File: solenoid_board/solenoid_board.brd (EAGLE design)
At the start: 39.4 x 38.1 mm, 28 parts, among them Q1 MOSFET-NCHANNELSMD, Q2 MOSFET-NCHANNELSMD, Q3 MOSFET-NCHANNELSMD, Q4 MOSFET-NCHANNELSMD

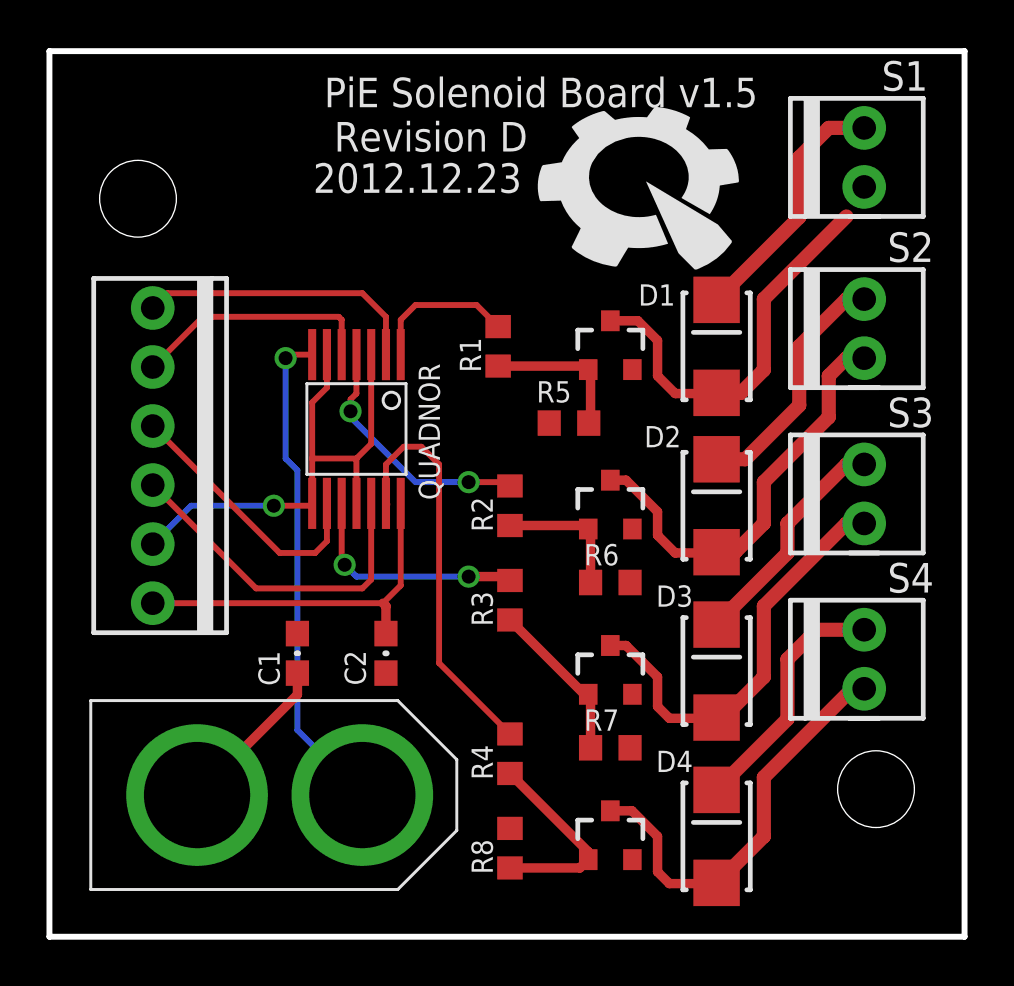
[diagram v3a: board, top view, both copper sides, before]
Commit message: Sherlock, Watson, and Solenoid Rev E
- Updated all parts on all boards with their new
  versions in pie.lbr
- Cleaned up silkscreens and made names more
  meaningful
- Cleaned up schematics

This is intended to be the final version for all
three boards. There will be one more revision,
but that is only to add the copyright info Ryan
is making for the schematics and boards.

A side-effect of cleaning up the schematics is
that some connections may have been severd and
traces may have disappeared. I've tried my best
to detect and re-route those traces. If you find
any, please let me know. Thanks.

Sherlock DFM: https://www.freedfm.com/freedfm/0019486703422743/results/summary2.htm
Watson DFM: https://www.freedfm.com/freedfm/0019486703422746/results/summary2.htm
Solenoid DFM: https://www.freedfm.com/freedfm/0019486703422817/results/summary2.htm

Change-Id: I0ddac82c4f4e303a663db72d1e0729480dfd451e
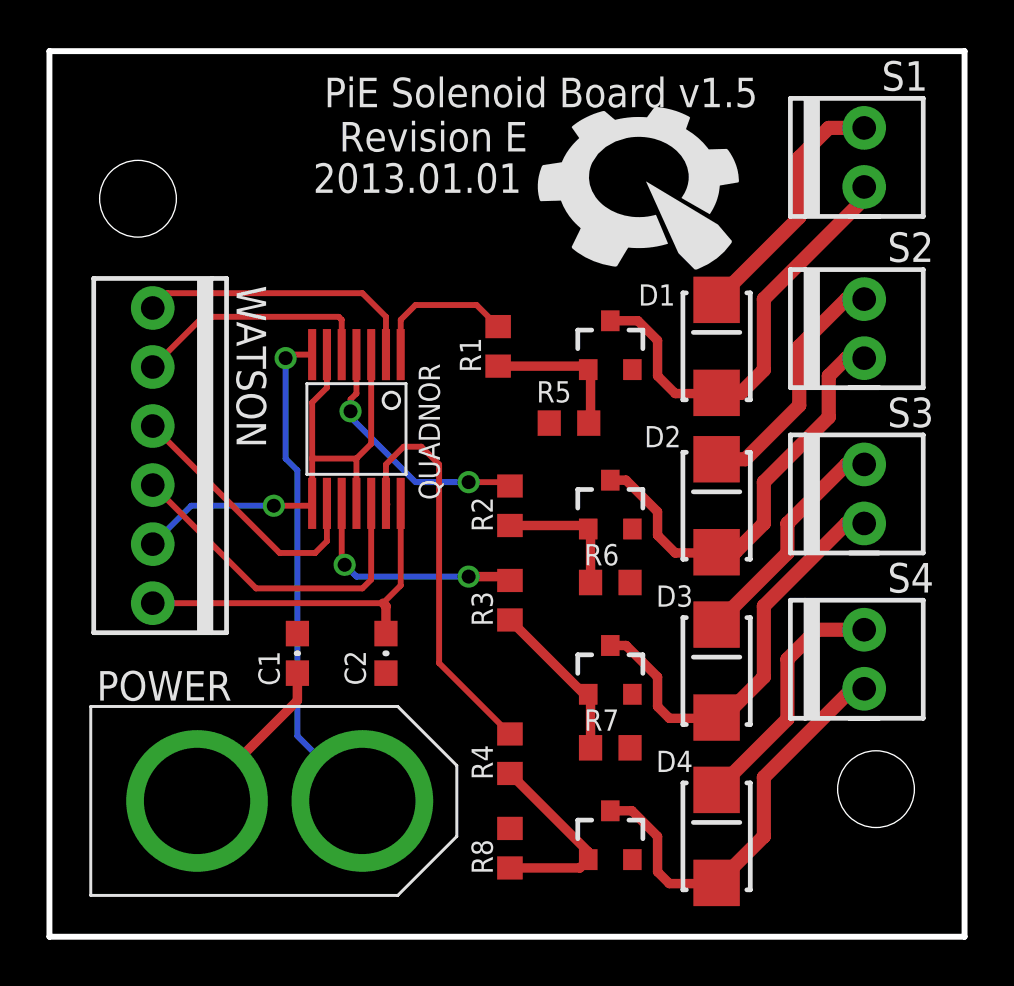
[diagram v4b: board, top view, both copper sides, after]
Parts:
- moved U$2 8.98 mm to (9.91, 5.84)
- moved S4 1.27 mm to (35.1, 11.9)
- moved S2 1.27 mm to (35.1, 26.2)
- moved S3 1.27 mm to (35.1, 19.1)
- moved S1 1.27 mm to (35.1, 33.5)
- renumbered SOL to WATSON
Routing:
- net N$2: track 17.3 -> 18.9 mm
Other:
- board text added: "2013.01.01"
- board text added: "POWER"
- board text added: "Revision E"
- board text removed: "2012.12.23"
- board text removed: "Revision D"
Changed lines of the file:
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@@
 <setting verticaltext="up"/>
 </settings>
-<grid distance="10" unitdist="mil" unit="inch" style="lines" multiple="1" display="yes" altdistance="0.025" altunitdist="inch" altunit="inch"/>
+<grid distance="0.01" unitdist="inch" unit="inch" style="lines" multiple="1" display="yes" altdistance="0.025" altunitdist="inch" altunit="inch"/>
 <layers>
 <layer number="1" name="Top" color="4" fill="1" visible="yes" active="yes"/>
@@
 <wire x1="0" y1="38.1" x2="0" y2="0" width="0.254" layer="20"/>
 <text x="30.48" y="36.957" size="1.27" layer="25" font="vector" ratio="20" rot="R180">PiE Solenoid Board v1.5</text>
-<text x="20.574" y="35.052" size="1.27" layer="21" font="vector" ratio="20" rot="R180">Revision D</text>
-<text x="20.32" y="33.274" size="1.27" layer="21" font="vector" ratio="20" rot="R180">2012.12.23</text>
+<text x="20.574" y="35.052" size="1.27" layer="21" font="vector" ratio="20" rot="R180">Revision E</text>
+<text x="20.32" y="33.274" size="1.27" layer="21" font="vector" ratio="20" rot="R180">2013.01.01</text>
+<text x="2.032" y="10.16" size="1.27" layer="21" font="vector" ratio="20">POWER</text>
 </plain>
 <attributes>
@@
 </element>
 <element name="U$1" library="pie" package="PIE-LOGO-SMALL" value="" x="25.654" y="32.512"/>
-<element name="U$2" library="pie" package="XT60CONNECTOR" value="XT60CONNECTOR" x="1.778" y="2.032">
-<attribute name="PARTNUMBER" value="PRT-10474 " x="1.778" y="2.032" size="1.778" layer="27" display="off"/>
-</element>
-<element name="SOL" library="pie" package="1X06-MTA" value="" x="4.445" y="20.701" smashed="yes" rot="R270">
-<attribute name="VALUE" x="1.397" y="15.748" size="1.27" layer="27" rot="R90"/>
+<element name="U$2" library="pie" package="XT60CONNECTOR" value="XT60CONNECTOR" x="9.906" y="5.842">
+<attribute name="PARTNUMBER" value="PRT-10474 " x="9.906" y="5.842" size="1.778" layer="27" display="off"/>
+</element>
+<element name="WATSON" library="pie" package="1X06-MTA" value="" x="4.445" y="20.701" smashed="yes" rot="R270">
 <attribute name="PARTNUMBER" value="A1923-ND" x="4.445" y="20.701" size="1.778" layer="27" rot="R270" display="off"/>
-</element>
-<element name="S1" library="pie" package="1X02-MTA" value="" x="35.052" y="32.258" smashed="yes" rot="R90">
+<attribute name="NAME" x="8.0518" y="28.0162" size="1.27" layer="25" font="vector" ratio="20" rot="SR270"/>
+<attribute name="VALUE" x="0" y="27.686" size="1.27" layer="27" font="vector" rot="R270"/>
+</element>
+<element name="S1" library="pie" package="1X02-MTA" value="" x="35.052" y="33.528" smashed="yes" rot="R90">
 <attribute name="NAME" x="37.7952" y="37.6682" size="1.27" layer="25" font="vector" ratio="20" rot="R180"/>
-<attribute name="VALUE" x="39.497" y="30.988" size="1.27" layer="27" rot="R90"/>
-<attribute name="PARTNUMBER" value="A1921-ND" x="35.052" y="32.258" size="1.778" layer="27" rot="R90" display="off"/>
-</element>
-<element name="S2" library="pie" package="1X02-MTA" value="" x="35.052" y="24.892" smashed="yes" rot="R90">
+<attribute name="VALUE" x="39.497" y="32.258" size="1.27" layer="27" rot="R90"/>
+<attribute name="PARTNUMBER" value="A1921-ND" x="35.052" y="33.528" size="1.778" layer="27" rot="R90" display="off"/>
+</element>
+<element name="S2" library="pie" package="1X02-MTA" value="" x="35.052" y="26.162" smashed="yes" rot="R90">
 <attribute name="NAME" x="38.0492" y="30.3022" size="1.27" layer="25" font="vector" ratio="20" rot="R180"/>
-<attribute name="VALUE" x="39.497" y="23.622" size="1.27" layer="27" rot="R90"/>
-<attribute name="PARTNUMBER" value="A1921-ND" x="35.052" y="24.892" size="1.778" layer="27" rot="R90" display="off"/>
-</element>
-<element name="S3" library="pie" package="1X02-MTA" value="" x="35.052" y="17.78" smashed="yes" rot="R90">
+<attribute name="VALUE" x="39.497" y="24.892" size="1.27" layer="27" rot="R90"/>
+<attribute name="PARTNUMBER" value="A1921-ND" x="35.052" y="26.162" size="1.778" layer="27" rot="R90" display="off"/>
+</element>
+<element name="S3" library="pie" package="1X02-MTA" value="" x="35.052" y="19.05" smashed="yes" rot="R90">
 <attribute name="NAME" x="38.0492" y="23.1902" size="1.27" layer="25" font="vector" ratio="20" rot="R180"/>
-<attribute name="VALUE" x="39.497" y="16.51" size="1.27" layer="27" rot="R90"/>
-<attribute name="PARTNUMBER" value="A1921-ND" x="35.052" y="17.78" size="1.778" layer="27" rot="R90" display="off"/>
-</element>
-<element name="S4" library="pie" package="1X02-MTA" value="" x="35.052" y="10.668" smashed="yes" rot="R90">
+<attribute name="VALUE" x="39.497" y="17.78" size="1.27" layer="27" rot="R90"/>
+<attribute name="PARTNUMBER" value="A1921-ND" x="35.052" y="19.05" size="1.778" layer="27" rot="R90" display="off"/>
+</element>
+<element name="S4" library="pie" package="1X02-MTA" value="" x="35.052" y="11.938" smashed="yes" rot="R90">
 <attribute name="NAME" x="38.0492" y="16.0782" size="1.27" layer="25" font="vector" ratio="20" rot="R180"/>
-<attribute name="VALUE" x="39.497" y="9.398" size="1.27" layer="27" rot="R90"/>
-<attribute name="PARTNUMBER" value="A1921-ND" x="35.052" y="10.668" size="1.778" layer="27" rot="R90" display="off"/>
+<attribute name="VALUE" x="39.497" y="10.668" size="1.27" layer="27" rot="R90"/>
+<attribute name="PARTNUMBER" value="A1921-ND" x="35.052" y="11.938" size="1.778" layer="27" rot="R90" display="off"/>
 </element>
 <element name="R5" library="pie" package="R0603" value="10k" x="22.352" y="22.098" smashed="yes">
@@
 <contactref element="U$2" pad="12V"/>
 <contactref element="C1" pad="1"/>
-<wire x1="10.668" y1="11.342" x2="10.668" y2="10.414" width="0.4064" layer="1"/>
-<wire x1="10.668" y1="10.414" x2="6.35" y2="6.096" width="0.4064" layer="1"/>
+<wire x1="10.668" y1="11.342" x2="10.668" y2="10.16" width="0.4064" layer="1"/>
 <contactref element="D2" pad="C"/>
 <contactref element="S2" pad="2"/>
@@
 <wire x1="31.75" y1="17.78" x2="34.29" y2="20.32" width="0.6096" layer="1"/>
 <wire x1="34.29" y1="20.32" x2="35.052" y2="20.32" width="0.6096" layer="1"/>
+<wire x1="10.668" y1="10.16" x2="6.35" y2="5.842" width="0.4064" layer="1"/>
 </signal>
 <signal name="N$15">
@@
 <wire x1="16.764" y1="20.32" x2="16.764" y2="11.772" width="0.254" layer="1"/>
 <wire x1="16.764" y1="11.772" x2="19.812" y2="8.724" width="0.254" layer="1"/>
-<wire x1="14.5415" y1="18.6055" x2="14.478" y2="18.644" width="0" layer="19" extent="1-1"/>
 <wire x1="14.478" y1="20.32" x2="14.478" y2="18.644" width="0.254" layer="1"/>
+<wire x1="14.478" y1="18.644" x2="14.478" y2="18.542" width="0.254" layer="1"/>
 </signal>
 <signal name="N$3" class="1">
@@
 <wire x1="10.16" y1="24.892" x2="10.16" y2="20.574" width="0.254" layer="16"/>
 <wire x1="10.16" y1="20.574" x2="10.668" y2="20.066" width="0.254" layer="16"/>
-<wire x1="10.668" y1="20.066" x2="10.668" y2="8.89" width="0.254" layer="16"/>
+<wire x1="10.668" y1="20.066" x2="10.668" y2="8.636" width="0.254" layer="16"/>
 <contactref element="C2" pad="2"/>
 <contactref element="U$2" pad="GND"/>
@@
 <contactref element="Q3" pad="2"/>
 <contactref element="Q4" pad="2"/>
-<wire x1="10.668" y1="8.89" x2="13.462" y2="6.096" width="0.254" layer="16"/>
+<wire x1="10.668" y1="8.636" x2="13.462" y2="5.842" width="0.254" layer="16"/>
 </signal>
 <signal name="N$2">
@@
 <wire x1="26.162" y1="25.654" x2="25.316" y2="26.5" width="0.4064" layer="1"/>
 <wire x1="25.316" y1="26.5" x2="24.13" y2="26.5" width="0.4064" layer="1"/>
-<wire x1="34.29" y1="30.988" x2="30.734" y2="27.432" width="0.6096" layer="1"/>
+<wire x1="35.052" y1="31.75" x2="30.734" y2="27.432" width="0.6096" layer="1"/>
 <wire x1="30.734" y1="27.432" x2="30.734" y2="24.384" width="0.6096" layer="1"/>
 <wire x1="30.734" y1="24.384" x2="29.75" y2="23.4" width="0.6096" layer="1"/>
 <wire x1="29.75" y1="23.4" x2="28.702" y2="23.4" width="0.6096" layer="1"/>
-<wire x1="34.29" y1="30.988" x2="35.052" y2="32.258" width="0" layer="19" extent="1-1"/>
+<wire x1="35.052" y1="31.75" x2="35.052" y2="32.258" width="0.6096" layer="1"/>
 </signal>
 <signal name="IO61">
-<contactref element="SOL" pad="5"/>
+<contactref element="WATSON" pad="5"/>
 <contactref element="QUADNOR" pad="1B"/>
 <contactref element="QUADNOR" pad="2B"/>
@@
 </signal>
 <signal name="VCC">
-<contactref element="SOL" pad="6"/>
+<contactref element="WATSON" pad="6"/>
 <contactref element="QUADNOR" pad="VCC"/>
 <wire x1="4.445" y1="14.351" x2="14.351" y2="14.351" width="0.254" layer="1"/>
@@
 </signal>
 <signal name="IO65">
-<contactref element="SOL" pad="4"/>
+<contactref element="WATSON" pad="4"/>
 <contactref element="QUADNOR" pad="4B"/>
 <wire x1="4.445" y1="19.431" x2="8.89" y2="14.986" width="0.254" layer="1"/>
@@
 </signal>
 <signal name="IO21">
-<contactref element="SOL" pad="3"/>
+<contactref element="WATSON" pad="3"/>
 <contactref element="QUADNOR" pad="3B"/>
 <wire x1="4.445" y1="21.971" x2="9.906" y2="16.51" width="0.254" layer="1"/>
@@
 </signal>
 <signal name="IO63">
-<contactref element="SOL" pad="2"/>
+<contactref element="WATSON" pad="2"/>
 <contactref element="QUADNOR" pad="2A"/>
 <wire x1="12.446" y1="26.67" x2="6.604" y2="26.67" width="0.254" layer="1"/>
@@
 </signal>
 <signal name="IO64">
-<contactref element="SOL" pad="1"/>
+<contactref element="WATSON" pad="1"/>
 <contactref element="QUADNOR" pad="1A"/>
 <wire x1="14.478" y1="26.67" x2="14.478" y2="25.1075" width="0.254" layer="1"/>

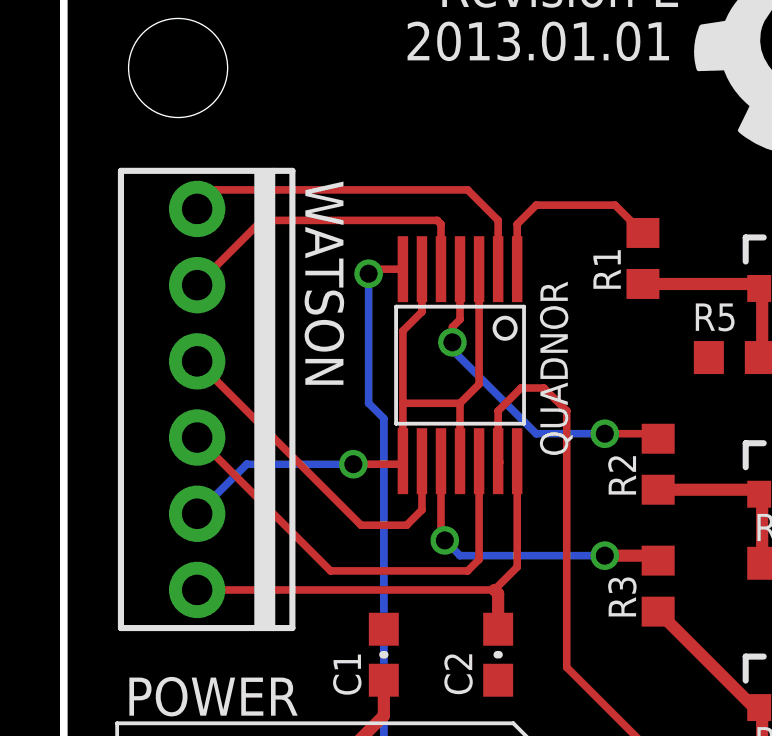
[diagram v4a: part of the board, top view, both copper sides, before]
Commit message: Sherlock/Watson/Solenoid Rev E (Again)
Had to make a few simple changes Dennis requested.
This is the final version. Rev F will only contain
extra copyright material.

Sherlcok DFM: https://www.freedfm.com/freedfm/0019486703424644/results/summary2.htm
Watson DFM: https://www.freedfm.com/freedfm/0019486703424641/results/summary2.htm
Solenoid DFM: https://www.freedfm.com/freedfm/0019486703424640/results/summary2.htm

Change-Id: Ibaa3e17f4a8e9033ce9bcff25cf747d321aea476
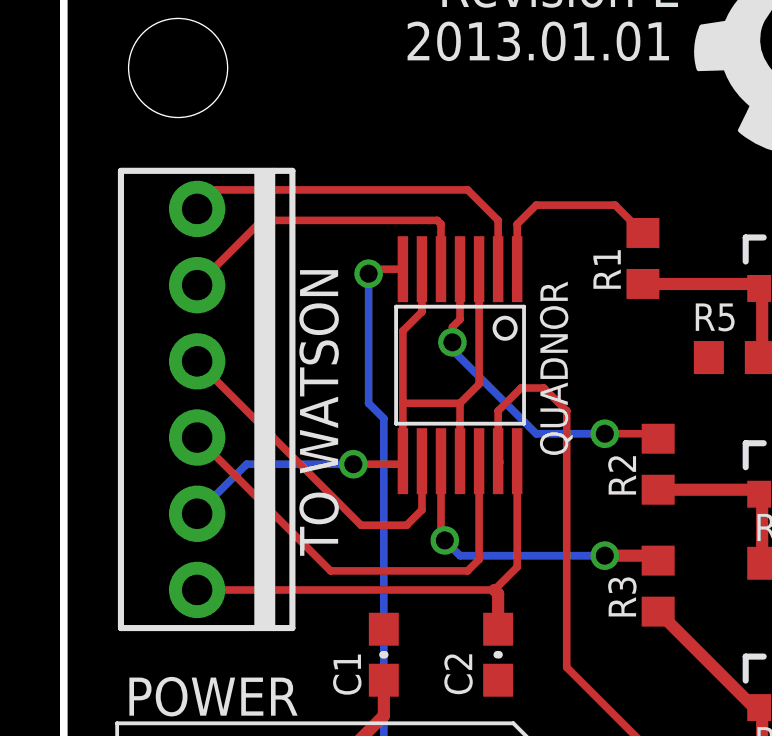
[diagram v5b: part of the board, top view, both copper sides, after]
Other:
- board text added: "TO WATSON"
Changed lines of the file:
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@@
 <setting verticaltext="up"/>
 </settings>
-<grid distance="0.01" unitdist="inch" unit="inch" style="lines" multiple="1" display="yes" altdistance="0.025" altunitdist="inch" altunit="inch"/>
+<grid distance="0.005" unitdist="inch" unit="inch" style="lines" multiple="1" display="yes" altdistance="0.025" altunitdist="inch" altunit="inch"/>
 <layers>
 <layer number="1" name="Top" color="4" fill="1" visible="yes" active="yes"/>
@@
 <text x="20.32" y="33.274" size="1.27" layer="21" font="vector" ratio="20" rot="R180">2013.01.01</text>
 <text x="2.032" y="10.16" size="1.27" layer="21" font="vector" ratio="20">POWER</text>
+<text x="9.144" y="15.494" size="1.27" layer="21" font="vector" ratio="20" rot="SR90">TO WATSON</text>
 </plain>
 <attributes>
@@
 <element name="WATSON" library="pie" package="1X06-MTA" value="" x="4.445" y="20.701" smashed="yes" rot="R270">
 <attribute name="PARTNUMBER" value="A1923-ND" x="4.445" y="20.701" size="1.778" layer="27" rot="R270" display="off"/>
-<attribute name="NAME" x="8.0518" y="28.0162" size="1.27" layer="25" font="vector" ratio="20" rot="SR270"/>
 <attribute name="VALUE" x="0" y="27.686" size="1.27" layer="27" font="vector" rot="R270"/>
 </element>
